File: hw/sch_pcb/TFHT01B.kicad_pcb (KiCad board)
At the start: 2 copper layers, 30 x 15 mm, 31 parts, among them J1 SM04B-GHS-TB, J2 SM04B-GHS-TB, M1 M3, M2 M3, M3 M3, M4 M3, M5 M3, M6 M3, M7 CAP-SF2, Q1 BC817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

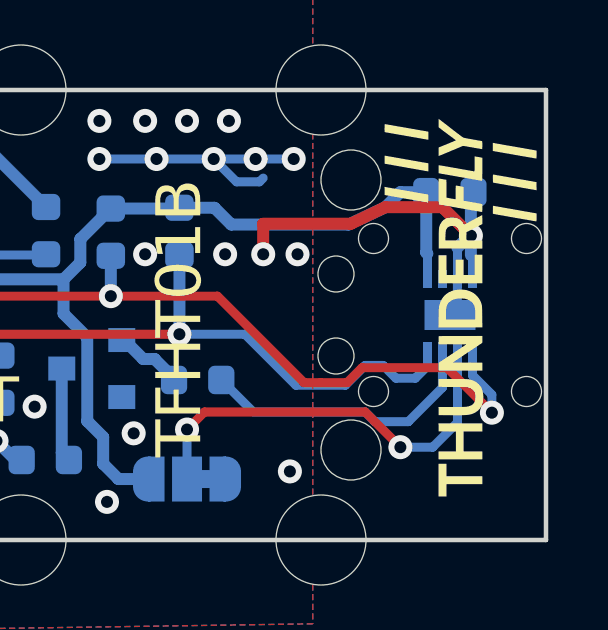
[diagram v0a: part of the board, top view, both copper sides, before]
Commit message: Change U1 footprint to KiCAD standard library footprint. The footprint respects Sensirion drawing from  the datasheet.
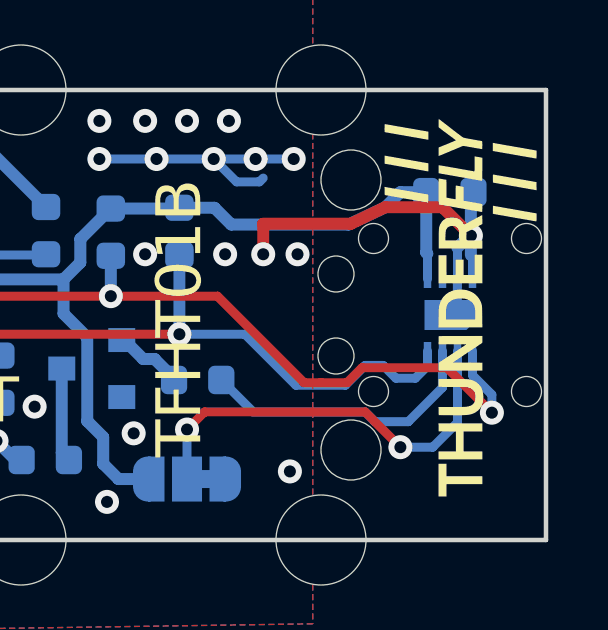
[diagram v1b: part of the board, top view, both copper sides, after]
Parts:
- U1: value SHT31 -> SHT31-DIS-B; footprint Mlab_IO:DFN-8-1EP_2.4x2.4mm_Pitch0.5mm -> Sensor_Humidity:Sensirion_DFN-8-1EP_2.5x2.5mm_P0.5mm_EP1.1x1.7mm
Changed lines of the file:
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@@
       (effects (font (size 1.27 1.27) (thickness 0.15)) (justify mirror))
     )
-    (fp_text user "K" (at 2.032 -0.0508 unlocked) (layer "F.Fab")
+    (fp_text user "K" (at 2.032 -0.0508 unlocked) (layer "F.Fab") hide
       (effects (font (size 1 1) (thickness 0.15)))
     )
@@
     (property "Sheetname" "")
     (property "UST_ID" "5c70984812875079b91f8bf2")
-    (property "UST_id" "")
     (attr smd)
     (fp_text reference "C4" (at 0 1.43 90) (layer "B.SilkS") hide
@@
     (property "Sheetname" "")
     (property "UST_ID" "60879d38128750769ee58e48")
-    (property "UST_id" "")
     (attr smd)
     (fp_text reference "D1" (at 0 1.3 90) (layer "B.SilkS") hide
@@
       (effects (font (size 1.27 1.27) (thickness 0.15)) (justify mirror))
     )
-    (fp_text user "K" (at 2.032 -0.0508 unlocked) (layer "F.Fab")
+    (fp_text user "K" (at 2.032 -0.0508 unlocked) (layer "F.Fab") hide
       (effects (font (size 1 1) (thickness 0.15)))
     )
@@
     )
   )
-  (footprint "Mlab_IO:DFN-8-1EP_2.4x2.4mm_Pitch0.5mm" (layer "B.Cu")
+  (footprint "Sensor_Humidity:Sensirion_DFN-8-1EP_2.5x2.5mm_P0.5mm_EP1.1x1.7mm" (layer "B.Cu")
     (at 26.8 -7.5 90)
-    (descr "DFN8 2x2, 0.5mm pin")
-    (tags "DFN 0.5")
+    (descr "Sensirion DFN-8 SHT3x-DIS (https://www.sensirion.com/fileadmin/user_upload/customers/sensirion/Dokumente/2_Humidity_Sensors/Datasheets/Sensirion_Humidity_Sensors_SHT3x_Datasheet_digital.pdf)")
+    (tags "sensirion dfn nolead")
     (property "Sheetfile" "TFHT01B.kicad_sch")
     (property "Sheetname" "")
     (property "UST_ID" "5c70984612875079b91f89e4")
     (attr smd)
-    (fp_text reference "U1" (at 0 2.075 90) (layer "B.Fab")
-      (effects (font (size 1 1) (thickness 0.15)) (justify mirror))
-    )
-    (fp_text value "SHT31" (at 0 -2.075 90) (layer "B.Fab") hide
-      (effects (font (size 1 1) (thickness 0.15)) (justify mirror))
-    )
-    (fp_text user "${REFERENCE}" (at 0 2.075 90) (layer "B.SilkS")
-      (effects (font (size 1 1) (thickness 0.15)) (justify mirror))
-    )
-    (fp_text user "*" (at -1.206 1.046 90) (layer "B.Fab")
-      (effects (font (size 1 1) (thickness 0.15)) (justify mirror))
-    )
-    (fp_line (start -1.2 -1.2) (end 1.2 -1.2) (layer "B.SilkS") (width 0.15))
-    (fp_line (start -1.2 1.2) (end 1.2 1.2) (layer "B.SilkS") (width 0.15))
-    (fp_line (start -1.4 -1.35) (end 1.4 -1.35) (layer "B.CrtYd") (width 0.05))
-    (fp_line (start -1.4 1.35) (end -1.4 -1.35) (layer "B.CrtYd") (width 0.05))
-    (fp_line (start -1.4 1.35) (end 1.4 1.35) (layer "B.CrtYd") (width 0.05))
-    (fp_line (start 1.4 1.35) (end 1.4 -1.35) (layer "B.CrtYd") (width 0.05))
-    (fp_line (start -1.2 -1.2) (end 1.2 -1.2) (layer "B.Fab") (width 0.15))
-    (fp_line (start -1.2 1.2) (end 1.2 1.2) (layer "B.Fab") (width 0.15))
-    (pad "1" smd rect locked (at -1.2 0.75 90) (size 0.6 0.3) (layers "B.Cu" "B.Paste" "B.Mask")
+    (fp_text reference "U1" (at 0 2.25 270) (layer "B.SilkS")
+      (effects (font (size 1 1) (thickness 0.15)) (justify mirror))
+    )
+    (fp_text value "SHT31-DIS-B" (at 0.169 4.046 270) (layer "B.Fab") hide
+      (effects (font (size 1 1) (thickness 0.15)) (justify mirror))
+    )
+    (fp_text user "${REFERENCE}" (at 0 0 270) (layer "B.Fab")
+      (effects (font (size 0.4 0.4) (thickness 0.06)) (justify mirror))
+    )
+    (fp_line (start -1.09 1.41) (end 0.65 1.41) (layer "B.SilkS") (width 0.12))
+    (fp_line (start -0.65 -1.41) (end 0.65 -1.41) (layer "B.SilkS") (width 0.12))
+    (fp_line (start -1.7 1.5) (end 1.7 1.5) (layer "B.CrtYd") (width 0.05))
+    (fp_line (start -1.7 -1.5) (end 1.7 -1.5) (layer "B.CrtYd") (width 0.05))
+    (fp_line (start 1.7 1.5) (end 1.7 -1.5) (layer "B.CrtYd") (width 0.05))
+    (fp_line (start -1.7 1.5) (end -1.7 -1.5) (layer "B.CrtYd") (width 0.05))
+    (fp_line (start -1.25 -1.25) (end -1.25 0.75) (layer "B.Fab") (width 0.1))
+    (fp_line (start 1.25 -1.25) (end -1.25 -1.25) (layer "B.Fab") (width 0.1))
+    (fp_line (start -1.25 0.75) (end -0.75 1.25) (layer "B.Fab") (width 0.1))
+    (fp_line (start 1.25 1.25) (end 1.25 -1.25) (layer "B.Fab") (width 0.1))
+    (fp_line (start -0.75 1.25) (end 1.25 1.25) (layer "B.Fab") (width 0.1))
+    (pad "" smd custom (at 0 0 90) (size 0.9 0.9) (layers "B.Paste")
+      (zone_connect 0)
+      (options (clearance outline) (anchor rect))
+      (primitives
+        (gr_poly (pts
+            (xy 0.45 -0.8)
+            (xy -0.45 -0.8)
+            (xy -0.45 0.53)
+            (xy -0.18 0.8)
+            (xy 0.45 0.8)
+          ) (width 0) (fill yes))
+      ))
+    (pad "1" smd rect (at -1.175 0.75 90) (size 0.55 0.25) (layers "B.Cu" "B.Paste" "B.Mask")
       (net 6 "/SDA") (pinfunction "SDA") (pintype "unspecified"))
-    (pad "2" smd rect locked (at -1.2 0.25 90) (size 0.6 0.3) (layers "B.Cu" "B.Paste" "B.Mask")
+    (pad "2" smd rect (at -1.175 0.25 90) (size 0.55 0.25) (layers "B.Cu" "B.Paste" "B.Mask")
       (net 9 "Net-(JP1-Pad2)") (pinfunction "ADDR") (pintype "unspecified"))
-    (pad "3" smd rect locked (at -1.2 -0.25 90) (size 0.6 0.3) (layers "B.Cu" "B.Paste" "B.Mask")
+    (pad "3" smd rect (at -1.175 -0.25 90) (size 0.55 0.25) (layers "B.Cu" "B.Paste" "B.Mask")
       (net 11 "/ALERT") (pinfunction "ALERT") (pintype "unspecified"))
-    (pad "4" smd rect locked (at -1.2 -0.75 90) (size 0.6 0.3) (layers "B.Cu" "B.Paste" "B.Mask")
+    (pad "4" smd rect (at -1.175 -0.75 270) (size 0.55 0.25) (layers "B.Cu" "B.Paste" "B.Mask")
       (net 7 "/SCL") (pinfunction "SCL") (pintype "unspecified"))
-    (pad "5" smd rect locked (at 1.2 -0.75 90) (size 0.6 0.3) (layers "B.Cu" "B.Paste" "B.Mask")
+    (pad "5" smd rect (at 1.175 -0.75 90) (size 0.55 0.25) (layers "B.Cu" "B.Paste" "B.Mask")
       (net 4 "+3V3") (pinfunction "VDD") (pintype "unspecified"))
-    (pad "6" smd rect locked (at 1.2 -0.25 90) (size 0.6 0.3) (layers "B.Cu" "B.Paste" "B.Mask")
+    (pad "6" smd rect (at 1.175 -0.25 90) (size 0.55 0.25) (layers "B.Cu" "B.Paste" "B.Mask")
       (net 12 "unconnected-(U1-Pad6)") (pinfunction "nRESET") (pintype "unspecified+no_connect"))
-    (pad "7" smd rect locked (at 1.2 0.25 90) (size 0.6 0.3) (layers "B.Cu" "B.Paste" "B.Mask")
+    (pad "7" smd rect (at 1.175 0.25 90) (size 0.55 0.25) (layers "B.Cu" "B.Paste" "B.Mask")
       (net 1 "GND") (pinfunction "GND") (pintype "unspecified"))
-    (pad "8" smd rect locked (at 1.2 0.75 90) (size 0.6 0.3) (layers "B.Cu" "B.Paste" "B.Mask")
+    (pad "8" smd rect (at 1.175 0.75 90) (size 0.55 0.25) (layers "B.Cu" "B.Paste" "B.Mask")
       (net 1 "GND") (pinfunction "GND") (pintype "unspecified"))
-    (pad "9" smd rect locked (at 0 0 90) (size 1 1.7) (layers "B.Cu" "B.Paste" "B.Mask")
-      (net 1 "GND") (pinfunction "GND") (pintype "unspecified") (solder_paste_margin_ratio -0.2))
-    (model "${KISYS3DMOD_MLAB}/SHT3x.STEP"
+    (pad "9" smd custom (at 0 0 90) (size 1 1) (layers "B.Cu" "B.Mask")
+      (net 1 "GND") (pinfunction "GND") (pintype "unspecified") (zone_connect 0)
+      (options (clearance outline) (anchor circle))
+      (primitives
+        (gr_poly (pts
+            (xy 0.5 -0.85)
+            (xy -0.5 -0.85)
+            (xy -0.5 0.55)
+            (xy -0.2 0.85)
+            (xy 0.5 0.85)
+          ) (width 0) (fill yes))
+      ))
+    (model "${KICAD6_3DMODEL_DIR}/Sensor_Humidity.3dshapes/Sensirion_DFN-8-1EP_2.5x2.5mm_P0.5mm_EP1.1x1.7mm.wrl"
       (offset (xyz 0 0 0))
       (scale (xyz 1 1 1))
@@
     (property "Sheetname" "")
     (property "UST_ID" "5c70984812875079b91f8bf2")
-    (property "UST_id" "")
     (attr smd)
     (fp_text reference "C5" (at 0 1.43) (layer "B.SilkS") hide
@@
     (property "Sheetname" "")
     (property "UST_ID" "5c70984812875079b91f8bc2")
-    (property "UST_id" "")
     (attr smd)
     (fp_text reference "C1" (at 0 1.43 90) (layer "B.SilkS") hide
@@
     (property "Sheetname" "")
     (property "UST_ID" "5c70984812875079b91f8bbd")
-    (property "UST_id" "")
     (attr smd)
     (fp_text reference "C3" (at -0.0485 0.021 90) (layer "B.Fab")
@@
     (property "Sheetname" "")
     (property "UST_ID" "5c7255e81287500b4e112ea2")
-    (property "UST_id" "")
     (attr smd)
     (fp_text reference "U3" (at 0 2.9 90) (layer "B.SilkS") hide
@@
     (property "Sheetname" "")
     (property "UST_ID" "5c70984512875079b91f8962")
-    (property "UST_id" "")
     (attr smd)
     (fp_text reference "R3" (at 0 1.43 90) (layer "B.SilkS") hide
@@
     (property "Sheetname" "")
     (property "UST_ID" "5c70984512875079b91f8962")
-    (property "UST_id" "")
     (attr smd)
     (fp_text reference "R10" (at 0 1.43 90) (layer "B.SilkS") hide
@@
       (effects (font (size 1 1) (thickness 0.15)) (justify mirror))
     )
-    (fp_text value "CAP-SF2" (at 0 -3.906 unlocked) (layer "B.Fab")
-      (effects (font (size 1 1) (thickness 0.15)) (justify mirror))
-    )
+    (fp_text value "CAP-SF2" (at 0.404 -4.281 unlocked) (layer "B.Fab")
+      (effects (font (size 1 1) (thickness 0.15)) (justify mirror))
+    )

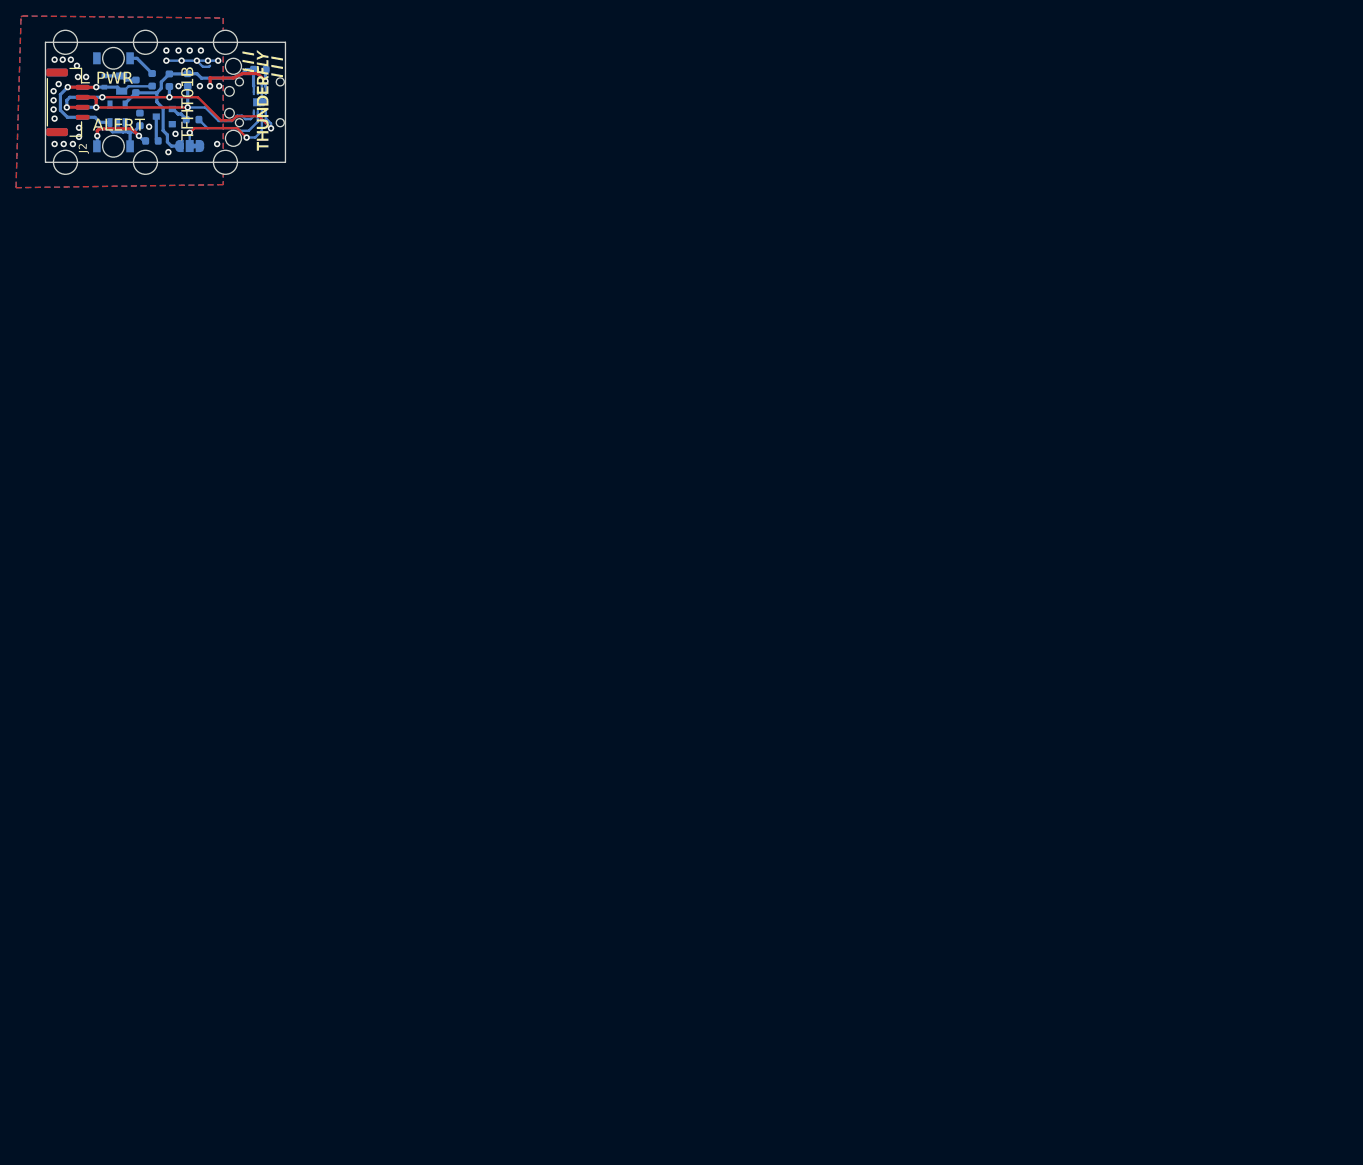
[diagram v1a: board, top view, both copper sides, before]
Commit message: Move PCB to the center of the page. Regenerate component placement drawing.
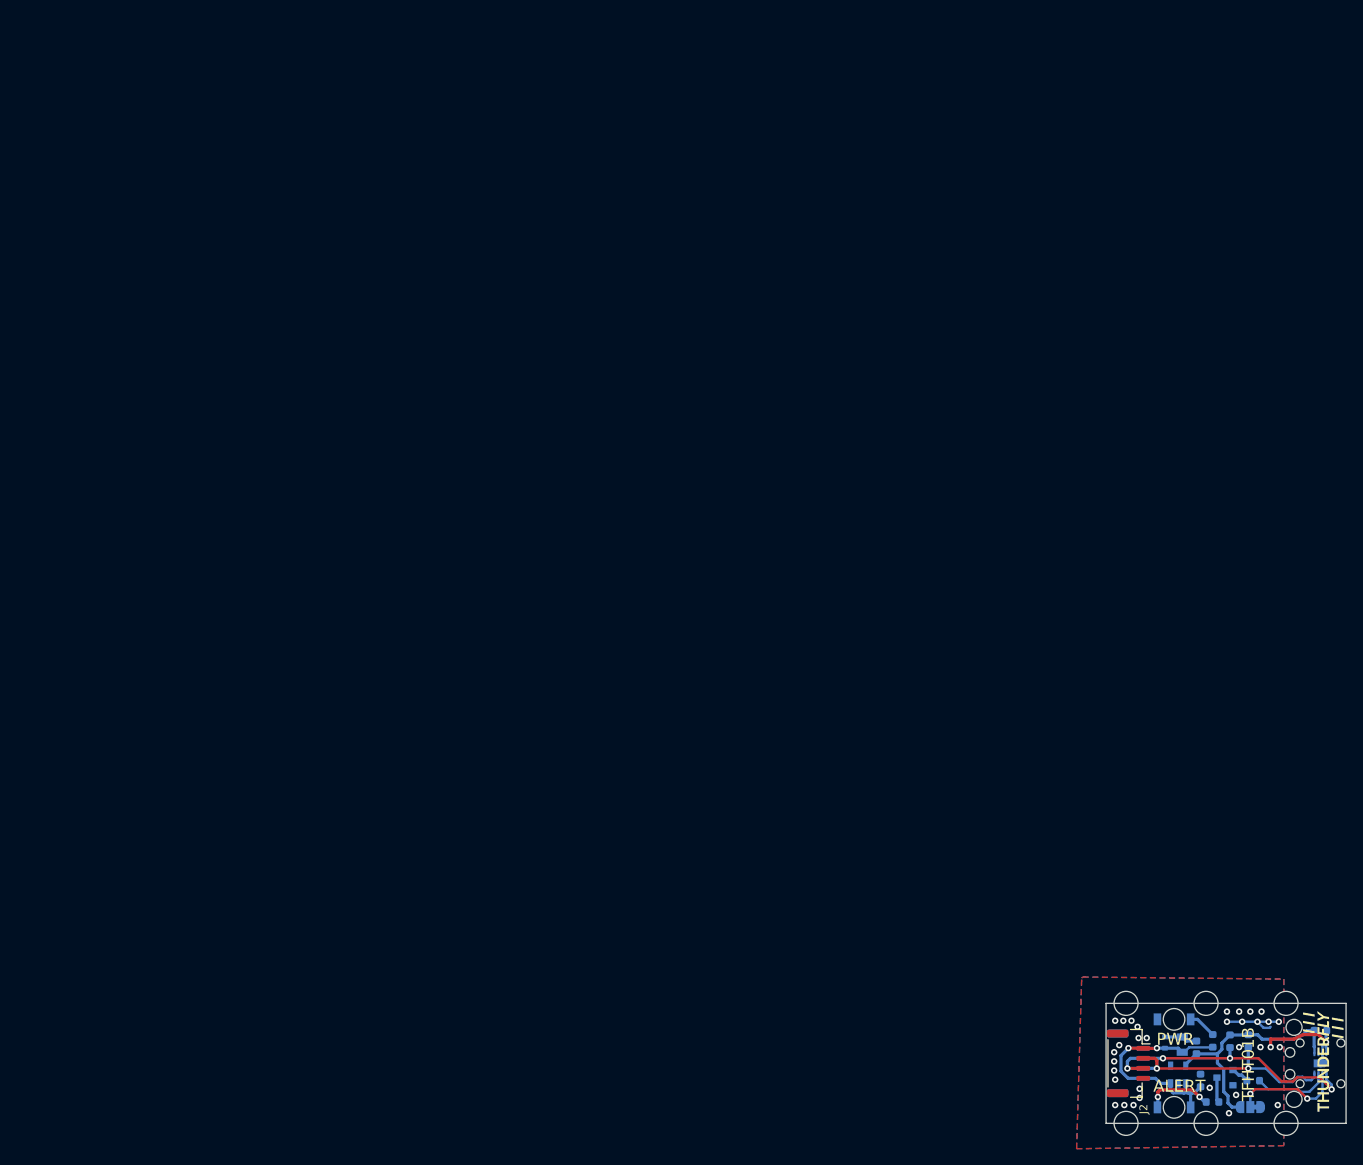
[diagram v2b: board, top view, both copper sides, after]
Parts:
- moved C1 178.9 mm to (143.9, 110.6)
- moved C3 178.9 mm to (142.1, 110.3)
- moved C4 178.9 mm to (144.4, 114.8)
- moved C5 178.9 mm to (159.4, 108.5)
- moved D1 178.9 mm to (139.9, 110.0)
- moved D2 178.9 mm to (141.1, 107.1)
- moved D3 178.9 mm to (141.1, 118.1)
- moved G*** 178.9 mm to (159.7, 112.5)
- moved J1 178.9 mm to (135.4, 112.6)
- moved J2 178.9 mm to (135.4, 112.6)
- moved JP1 178.9 mm to (150.6, 118.1)
- moved M1 178.9 mm to (155.1, 105.1)
- moved M2 178.9 mm to (145.1, 120.1)
- moved M3 178.9 mm to (135.1, 120.1)
- moved M4 178.9 mm to (145.1, 105.1)
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
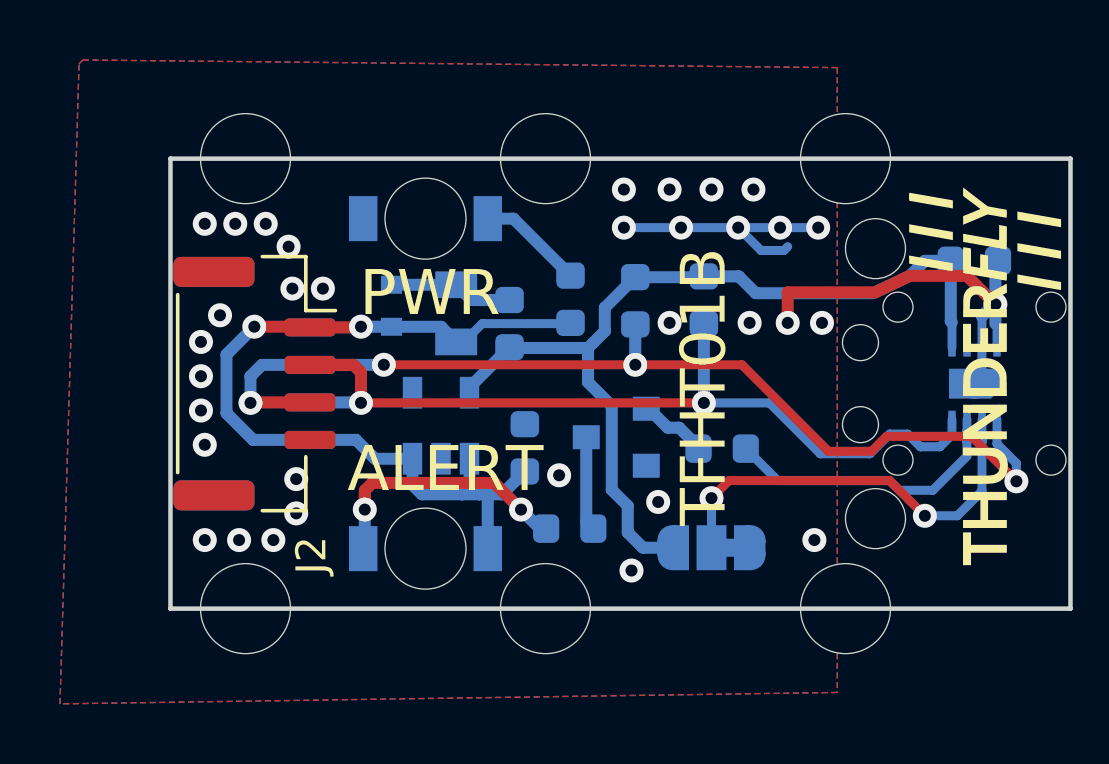
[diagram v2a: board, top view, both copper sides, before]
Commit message: Remove unecessary copper  #7
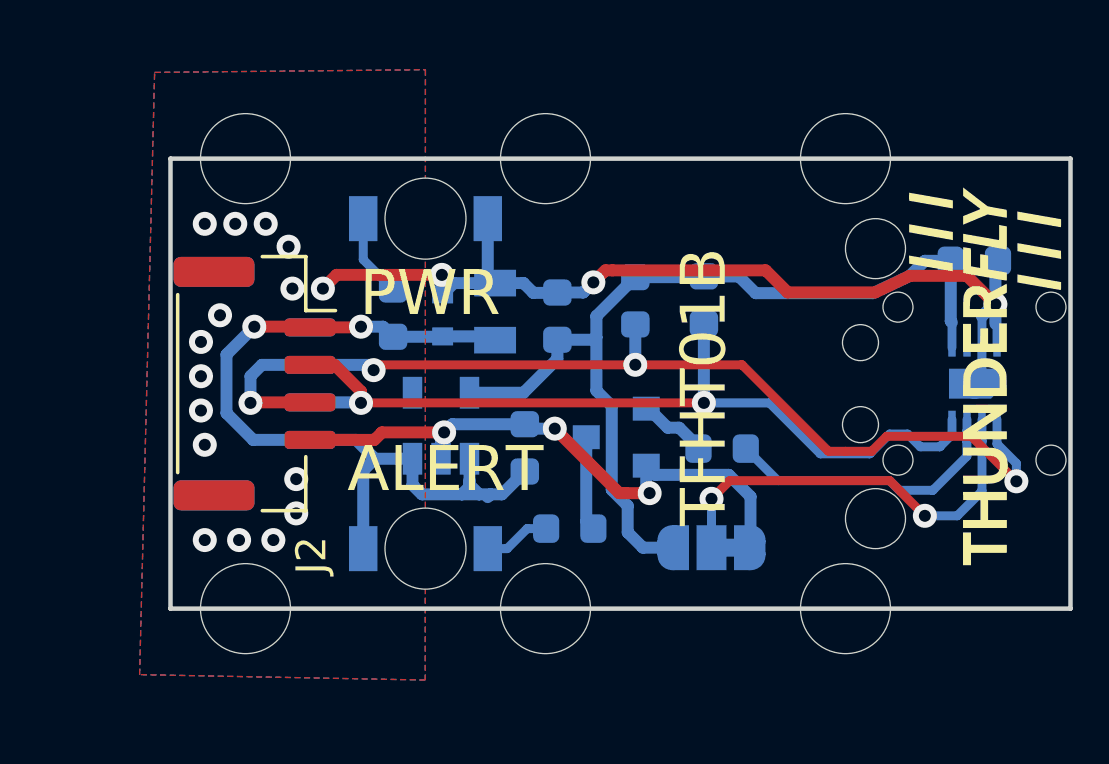
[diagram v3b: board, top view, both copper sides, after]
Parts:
- moved R1 5.93 mm to (140.0, 110.3)
- moved D1 1.73 mm to (141.6, 110.4)
- moved C1 1.61 mm to (145.5, 110.4)
- moved C3 1.30 mm to (143.4, 110.2)
- turned D2 to 0 degrees
- turned D3 to 0 degrees
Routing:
- net GND: track 27.3 -> 53.1 mm, vias 34 -> 22
- net Net-(D3-Pad1): track 8.74 -> 2.43 mm, vias 2 -> 0
- net +5V: track 29.9 -> 28.6 mm
- net Net-(D2-Pad2): track 3.55 -> 2.78 mm
- net +3V3: track 30.1 -> 30.7 mm
